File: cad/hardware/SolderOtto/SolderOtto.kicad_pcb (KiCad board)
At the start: 2 copper layers, 125 x 68 mm, 225 parts, among them J201 Conn_02x04_Counter_Clockwise, J202 Conn_01x02, J302 Conn_ARM_SWD_TagConnect_TC2030, J401 Conn_01x20, J501 Conn_01x05, J601 Conn_01x07, P301 USB_C_Plug_USB2.0, Q201 T2N7002AK, Q202 BC858B, Q203 BC847A, Q204 BC847A, Q601 Q_Dual_NMOS, Q602 Q_Dual_NMOS, Q603 DTD123EK, Q604 DTD123EK, Q605 BC847A, Q606 BC858B, Q607 BC847A, SW301 SW_Push, U201 LMR38010, U202 AP3211K, U203 AP3211K, U204 TPS63710, U205 MCP9701T-E/TT, U301 USBLC6-2SC6, U302 STM32G474RETx, U303 MX25R3235FM1xx0, U601 OPA2186, U602 VOM1271, U603 VOM1271, U604 TMUX4053, U605 OPA2186, U606 TMUX4053, U607 OPA202, U608 OPA2186, Y301 32.768 kHz

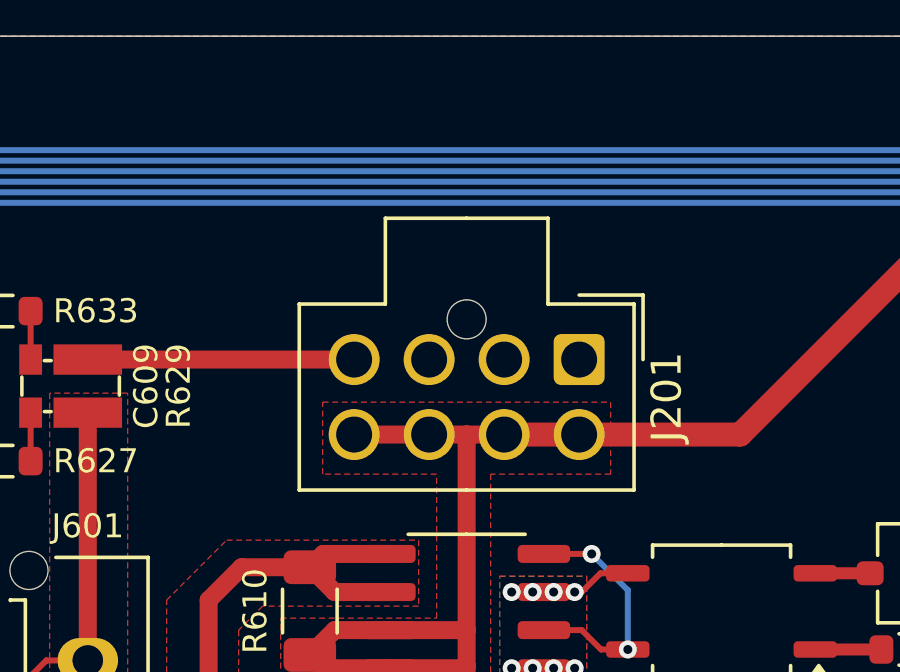
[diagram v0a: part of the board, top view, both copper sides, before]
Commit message: Implements basic ADC and display functionality
This commit sets up the basic application framework.

It adds wave control initialization, display functionality using BT81x, and ADC configurations for voltage and temperature measurements.
Also, it adds include directories and source files to CMakeLists, as well as fixes git ignore and device tree configurations.
The removal of the previous main.c and addition of separate c files allows for better modularity and organization.
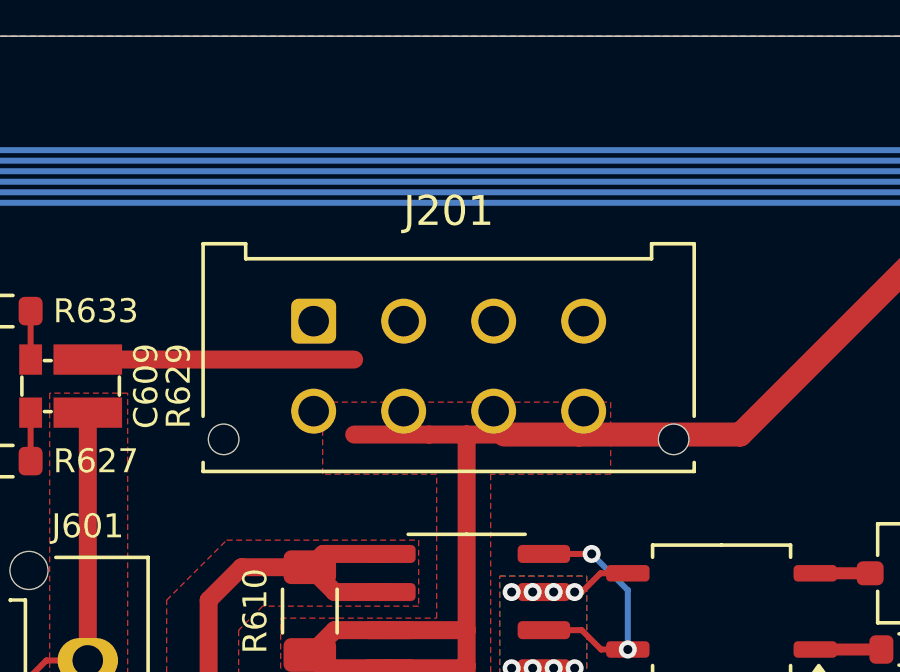
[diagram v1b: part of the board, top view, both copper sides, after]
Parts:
- J201: footprint Connector_Molex:Molex_Nano-Fit_105310-xx08_2x04_P2.50mm_Vertical -> Connector_Molex:Molex_Micro-Fit_3.0_43045-0812_2x04_P3.00mm_Vertical
- moved J201 8.94 mm to (121.5, 59.5), turned to 0 degrees
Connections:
- U303 pad 1: /mcu/QSPI_CLK -> /mcu/QSPI_NCS
- U303 pad 6: /mcu/QSPI_NCS -> /mcu/QSPI_CLK
